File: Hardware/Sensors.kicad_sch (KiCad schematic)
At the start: 0 parts

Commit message: Edited schematics
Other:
- company: (none) -> Burocket
- title: (none) -> Sensors
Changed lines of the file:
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@@
 	(generator_version "10.0")
 	(paper "A4")
+	(title_block
+		(title "Sensors")
+		(date "2026-07-08")
+		(rev "0.1")
+		(company "Burocket")
+	)
 	(text "[1] Sensors"
 		(exclude_from_sim no)

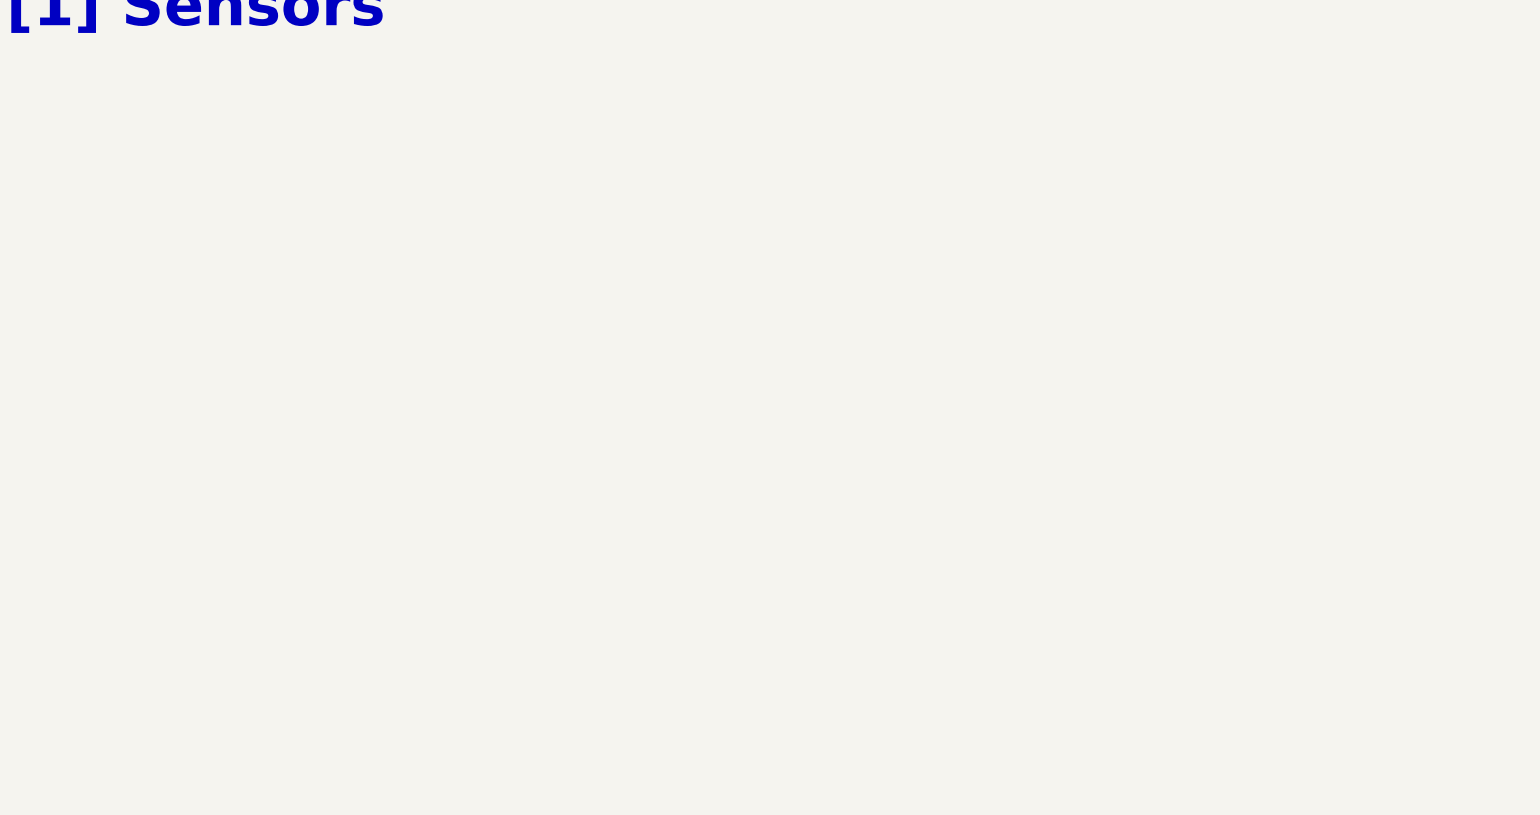
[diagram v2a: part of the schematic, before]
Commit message: Only SSR and ferrite bead selection is left
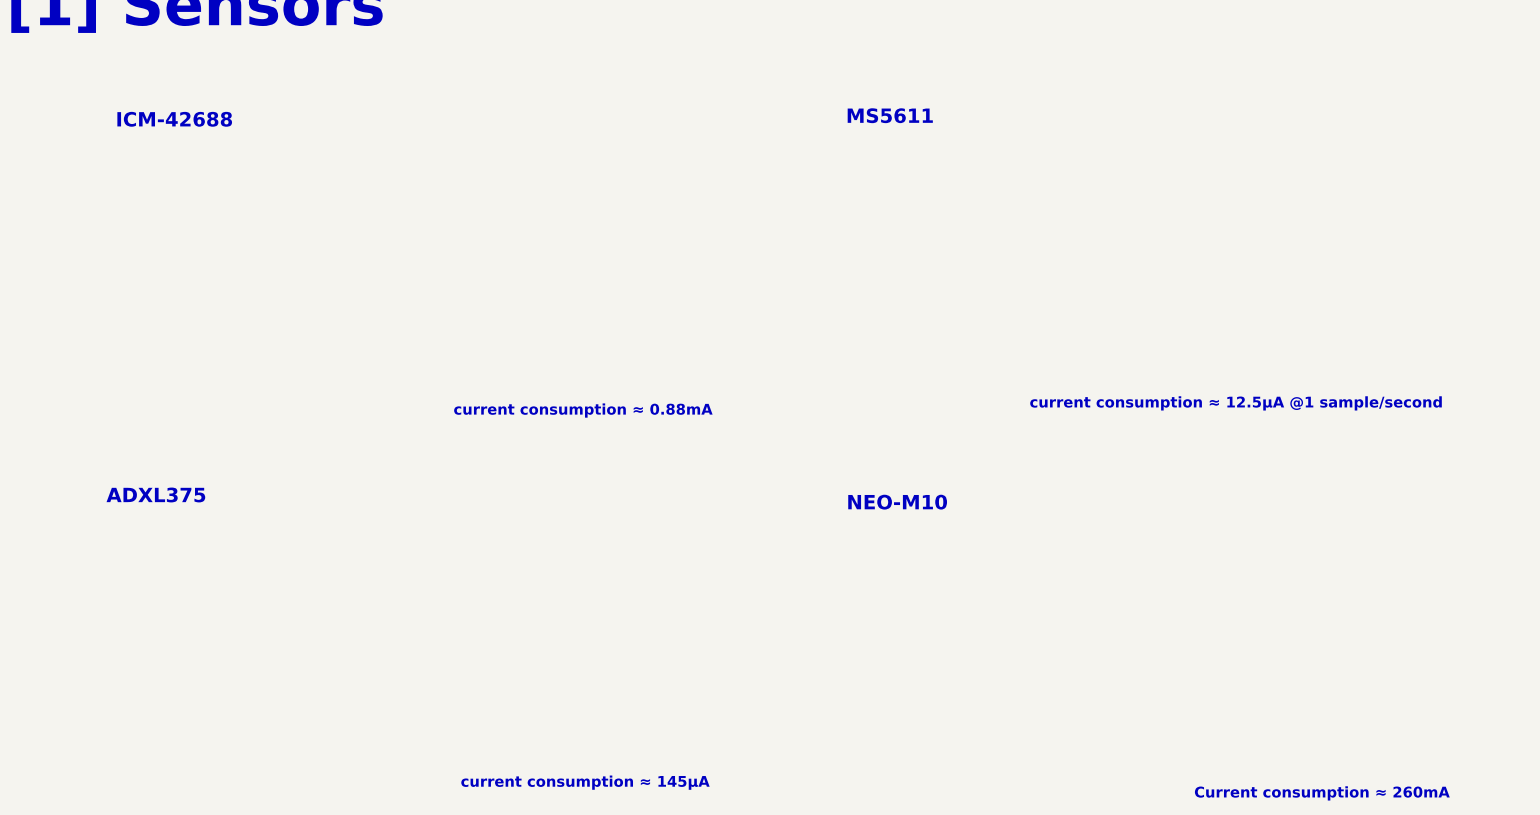
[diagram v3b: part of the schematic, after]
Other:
- note added: "ADXL375"
- note added: "Current consumption ≈ 260mA"
- note added: "ICM-42688"
- note added: "MS5611"
- note added: "NEO-M10"
- note added: "current consumption ≈ 0.88mA"
- note added: "current consumption ≈ 12.5µA @1 sample/second"
- note added: "current consumption ≈ 145µA"
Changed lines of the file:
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@@
 		(company "Burocket")
 	)
+	(text "current consumption ≈ 12.5µA @1 sample/second"
+		(exclude_from_sim no)
+		(at 193.04 89.535 0)
+		(effects
+			(font
+				(size 1.905 1.905)
+				(thickness 0.254)
+				(bold yes)
+			)
+			(justify left)
+		)
+	)
+	(text "ICM-42688"
+		(exclude_from_sim no)
+		(at 41.275 39.37 0)
+		(effects
+			(font
+				(size 2.54 2.54)
+				(thickness 0.508)
+				(bold yes)
+			)
+		)
+	)
 	(text "[1] Sensors"
 		(exclude_from_sim no)
@@
 		)
 	)
+	(text "NEO-M10"
+		(exclude_from_sim no)
+		(at 169.545 107.315 0)
+		(effects
+			(font
+				(size 2.54 2.54)
+				(thickness 0.508)
+				(bold yes)
+			)
+		)
+	)
+	(text "current consumption ≈ 145µA"
+		(exclude_from_sim no)
+		(at 92.075 156.845 0)
+		(effects
+			(font
+				(size 1.905 1.905)
+				(thickness 0.254)
+				(bold yes)
+			)
+			(justify left)
+		)
+	)
+	(text "current consumption ≈ 0.88mA"
+		(exclude_from_sim no)
+		(at 90.805 90.805 0)
+		(effects
+			(font
+				(size 1.905 1.905)
+				(thickness 0.254)
+				(bold yes)
+			)
+			(justify left)
+		)
+	)
+	(text "MS5611"
+		(exclude_from_sim no)
+		(at 168.275 38.735 0)
+		(effects
+			(font
+				(size 2.54 2.54)
+				(thickness 0.508)
+				(bold yes)
+			)
+		)
+	)
+	(text "Current consumption ≈ 260mA"
+		(exclude_from_sim no)
+		(at 222.25 158.75 0)
+		(effects
+			(font
+				(size 1.905 1.905)
+				(thickness 0.254)
+				(bold yes)
+			)
+			(justify left)
+		)
+	)
+	(text "ADXL375"
+		(exclude_from_sim no)
+		(at 38.1 106.045 0)
+		(effects
+			(font
+				(size 2.54 2.54)
+				(thickness 0.508)
+				(bold yes)
+			)
+		)
+	)
 	(image
 		(at 276.86 173.99)
@@
 		)
 	)
+	(rule_area
+		(exclude_from_sim no)
+		(in_bom yes)
+		(on_board yes)
+		(dnp no)
+		(polyline
+			(pts
+				(xy 29.21 102.87) (xy 29.21 159.385) (xy 137.795 159.385) (xy 137.795 102.87)
+			)
+			(stroke
+				(width 0)
+				(type dash)
+			)
+			(fill
+				(type none)
+			)
+		)
+	)
+	(rule_area
+		(exclude_from_sim no)
+		(in_bom yes)
+		(on_board yes)
+		(dnp no)
+		(polyline
+			(pts
+				(xy 159.385 104.14) (xy 159.385 160.655) (xy 267.97 160.655) (xy 267.97 104.14)
+			)
+			(stroke
+				(width 0)
+				(type dash)
+			)
+			(fill
+				(type none)
+			)
+		)
+	)
+	(rule_area
+		(exclude_from_sim no)
+		(in_bom yes)
+		(on_board yes)
+		(dnp no)
+		(polyline
+			(pts
+				(xy 159.385 35.56) (xy 159.385 92.075) (xy 267.97 92.075) (xy 267.97 35.56)
+			)
+			(stroke
+				(width 0)
+				(type dash)
+			)
+			(fill
+				(type none)
+			)
+		)
+	)
+	(rule_area
+		(exclude_from_sim no)
+		(in_bom yes)
+		(on_board yes)
+		(dnp no)
+		(polyline
+			(pts
+				(xy 29.21 36.195) (xy 29.21 92.71) (xy 137.795 92.71) (xy 137.795 36.195)
+			)
+			(stroke
+				(width 0)
+				(type dash)
+			)
+			(fill
+				(type none)
+			)
+		)
+	)

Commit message: Updated schematics
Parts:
- added C14, C20: 2.2uF, Capacitor_SMD:C_0402_1005Metric, symbol Device:C
- added C19, C26, C8, C9: 100nF, Capacitor_SMD:C_0402_1005Metric, symbol Device:C
- added R54, R55, R56: 10k, Resistor_SMD:R_0402_1005Metric, symbol Device:R
- added R57, R58, R59: 22, Resistor_SMD:R_0402_1005Metric, symbol Device:R
- added U5: MS5611-01BA, Package_LGA:LGA-8_3x5mm_P1.25mm, symbol Sensor_Pressure:MS5611-01BA
- added U6: ICM-42688-P, LGA14_2P5X3X0P91_TDK, symbol 2026-06-16_08-50-59:ICM-42688-P
- added U7: ADXL375BCCZ-RL7, ADXL375BCCZ_RL7:LGA_CC-14-1_ADI, symbol 2026-07-20_16-43-50:ADXL375BCCZ-RL7
- added U9: MAX-M10M-00B, MAX_M10M_00B:MOD18_MAX-M10M_UBL, symbol 2026-07-20_17-18-28:MAX-M10M-00B
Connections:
- net ADXL_SS: now also R56.2, U7.7 (*CS)
- net Acc_Gyro_CLK: now also R57.2, R58.2
- net Acc_Gyro_MISO: now also U6.1 (AP_SDO/AP_AD0), U7.12 (SDO/ALTADDRESS)
- net Acc_Gyro_MOSI: now also U6.14 (AP_SDIO/AP_SDI), U7.13 (SDA/SDI/SDIO)
- net BARO_MISO: now also U5.6 (SDO)
- net BARO_MOSI: now also U5.7 (SDI/SDA)
- net BARO_SCK: now also R59.2
- net BARO_SS: now also R54.2, U5.4 (CSB), U5.5 (CSB)
- net ICM_SS: now also R55.2, U6.12 (AP_CS)
- new net: R59.1, U5.8 (SCLK)
- new net: R58.1, U7.14 (SCL/SCLK)
- new net: R57.1, U6.13 (AP_SCL/AP_SCLK)
- new net +3.3V: C14.1, C19.1, C20.1, C26.1, C8.1, C9.1, R54.1, R55.1, R56.1, U5.1 (VDD), U6.5 (VDDIO), U6.8 (VDD), U7.1 (VDDI/O), U7.6 (VS), U9.14 (VCC_RF), U9.7 (V_IO), U9.8 (VCC)
- new net GND: C14.2, C19.2, C20.2, C26.2, C8.2, C9.2, U5.2 (PS), U5.3 (GND), U6.10 (RESV), U6.11 (RESV), U6.2 (RESV), U6.3 (RESV), U6.6 (GND), U6.7 (RESV), U6.9 (INT2/FSYNC/CLKIN), U7.10 (NC), U7.11 (RESERVED), U7.2 (GND), U7.4 (GND), U7.5 (GND), U9.1 (GND), U9.10 (GND), U9.12 (GND)
- no-connect marks 0 -> 4

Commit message: Commit bulamadim :)
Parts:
- removed U9: MAX-M10M-00B, MAX_M10M_00B:MOD18_MAX-M10M_UBL, symbol 2026-07-20_17-18-28:MAX-M10M-00B
- added AE1: Antenna, Connector_Coaxial:SMA_Amphenol_132134-10_Vertical, symbol Device:Antenna
- added C32: 0.1nF, Capacitor_SMD:C_0402_1005Metric, symbol Device:C
- added C33: 100nF, Capacitor_SMD:C_0402_1005Metric, symbol Device:C
- added C48: 22uF, Capacitor_SMD:C_0805_2012Metric, symbol Device:C
- added D8: Red LED, Capacitor_SMD:C_0603_1608Metric, symbol Device:LED
- added Q7: BCR116, Package_TO_SOT_SMD:SOT-23-3, symbol Transistor_BJT:DTC143Z
- added R65: 1k, Resistor_SMD:R_0402_1005Metric, symbol Device:R
- added U9: MAX-M10N, RF_GPS:ublox_MAX, symbol 2026-03-10_07-36-19:MAX-M10N
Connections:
- net +3.3V: now also C32.1, C33.1, C48.1, R65.1, U9.7 (V_IO), U9.8 (VCC)
- net GND: now also C32.2, C33.2, C48.2, Q7.2 (E), U9.1 (GND), U9.10 (GND), U9.12 (GND)
- new net: AE1.1 (A), U9.11 (RF_IN)
- new net: U9.16 (RESERVED), U9.17 (RESERVED)
- new net: D8.1 (K), Q7.3 (C)
- new net: D8.2 (A), R65.2
- new net GPS_EXTI: U9.5 (EXTI)
- new net GPS_RESET: U9.9 (RESET_N)
- new net GPS_RX: U9.2 (TX)
- new net GPS_TX: U9.3 (RX)
- new net TP: Q7.1 (B), U9.4 (TIMEPULSE)
- no-connect marks 4 -> 9
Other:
- note added: "- Consider A TVS diode for RF_IN line - Select a SMA or whatever RF connector: Impedance = 50ohm"
- note added: "Current consumption ≈ 100mA for inrush current"
- note added: "MAX-M10N"
- note removed: "Current consumption ≈ 260mA"
- note removed: "NEO-M10"

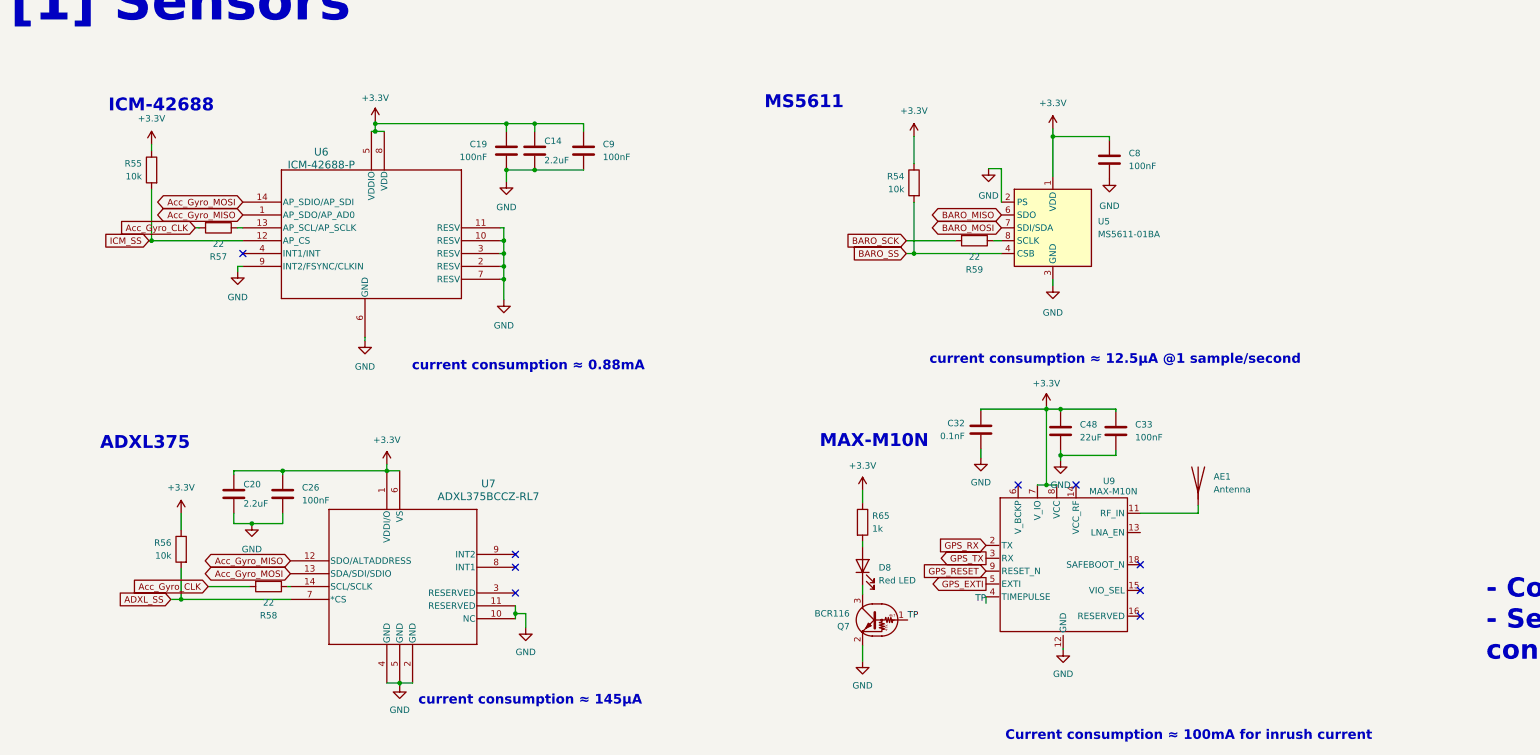
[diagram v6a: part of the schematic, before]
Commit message: Added New file for additional resources used, Changed LDO for lower noise, changed buck converter for higher switching speed, smaller inductance value, better transient current response
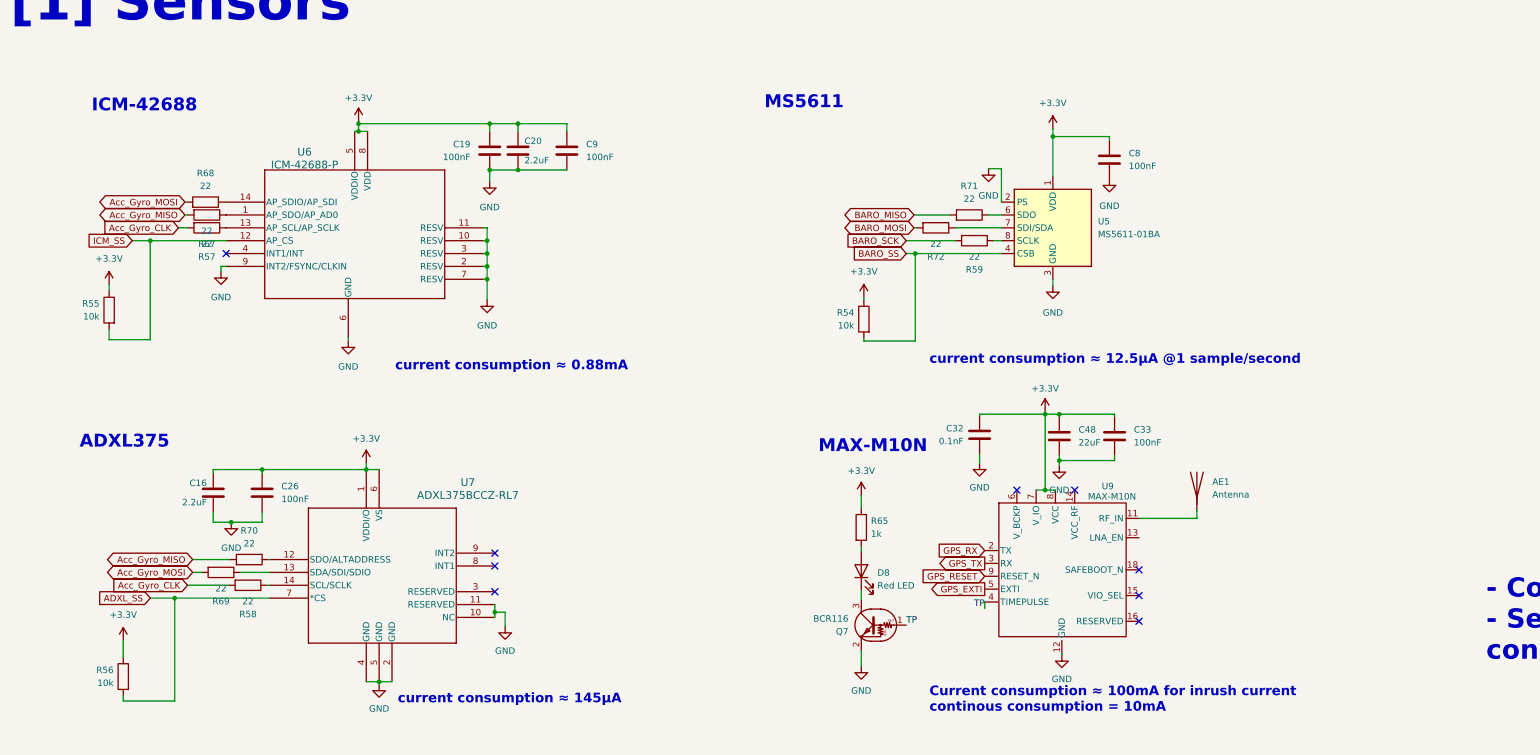
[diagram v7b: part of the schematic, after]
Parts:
- removed C14: 2.2uF, Capacitor_SMD:C_0402_1005Metric, symbol Device:C
- added C16: 2.2uF, Capacitor_SMD:C_0603_1608Metric, symbol Device:C
- added R67, R68, R69, R70, R71, R72: 22, Resistor_SMD:R_0402_1005Metric, symbol Device:R
- C20: footprint Capacitor_SMD:C_0402_1005Metric -> Capacitor_SMD:C_0603_1608Metric; Distributer Link http://ozdisan.com/p/smt-smd-ve-mlcc-kapasitorler-184/murat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 -> https://www.ozdisan.com/p/smt-smd-ve-mlcc-kapasitorler-184/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; Part Number GRT155C81A225ME13D -> CL10B225KP8NNNC
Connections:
- net +3.3V: now also C16.1
- net Acc_Gyro_MISO: now also R67.2, R70.2; no longer U6.1 (AP_SDO/AP_AD0), U7.12 (SDO/ALTADDRESS)
- net Acc_Gyro_MOSI: now also R68.2, R69.2; no longer U6.14 (AP_SDIO/AP_SDI), U7.13 (SDA/SDI/SDIO)
- net BARO_MISO: now also R71.2; no longer U5.6 (SDO)
- net BARO_MOSI: now also R72.2; no longer U5.7 (SDI/SDA)
- net GND: now also C16.2
- new net: R70.1, U7.12 (SDO/ALTADDRESS)
- new net: R68.1, U6.14 (AP_SDIO/AP_SDI)
- new net: R72.1, U5.7 (SDI/SDA)
- new net: R69.1, U7.13 (SDA/SDI/SDIO)
- new net: R71.1, U5.6 (SDO)
- new net: R67.1, U6.1 (AP_SDO/AP_AD0)
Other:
- note added: "Current consumption ≈ 100mA for inrush current continous consumption = 10mA"
- note removed: "Current consumption ≈ 100mA for inrush current"
- moved on the sheet: AE1, C19, C26, C32, C33, C48, C9, Q7, R54, R55, R56, R57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
